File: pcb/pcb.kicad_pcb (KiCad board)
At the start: 2 copper layers, 190.5 x 85.7 mm, 55 parts, among them J1 OLED, SW1 Rotary_Encoder_Switch, U1 Elite-C

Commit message: Added initial modified files.
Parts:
- removed D1, D10, D11, D12, D13, D14, D15, D16, D2, D3, D4, D5, D6, D7, D8, D9: BAV70, Keebio-Parts:SOT-23_Handsoldering
- removed MX00, MX01, MX03, MX10, MX11, MX12, MX20, MX21, MX22, MX30, MX31, MX32, MX40, MX41, MX42, MX43, MX50, MX51, MX53, MX60, MX62, MX63, MX71, MX72: MX-NoLED, MX_Only:MXOnly-1U-Hotswap
- removed MX02, MX61: MX-NoLED, MX_Only:MXOnly-1.5U-Hotswap
- removed MX13, MX33: MX-NoLED, MX_Only:MXOnly-1.25U-Hotswap
- removed MX23: MX-NoLED, MX_Only:MXOnly-3U-Hotswap
- removed MX52: MX-NoLED, MX_Only:MXOnly-2U-Hotswap
- U1: footprint Keebio-Parts:Elite-C-castellated-29pin-holes -> Keebio-Parts:Elite-C
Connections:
- SW1 pad S1: Col7 -> unconnected-(SW1-PadS1)
- SW1 pad S2: Net-(D13-Pad2) -> unconnected-(SW1-PadS2)
- U1 pad 1: Col0 -> unconnected-(U1-Pad1)
- U1 pad 10: Col7 -> unconnected-(U1-Pad10)
- U1 pad 11: Row2 -> unconnected-(U1-Pad11)
- U1 pad 12: Row1 -> unconnected-(U1-Pad12)
- U1 pad 13: Row3 -> unconnected-(U1-Pad13)
- U1 pad 16: Col6 -> unconnected-(U1-Pad16)
- U1 pad 17: Col5 -> unconnected-(U1-Pad17)
- U1 pad 18: Col4 -> unconnected-(U1-Pad18)
- U1 pad 19: Col3 -> unconnected-(U1-Pad19)
- U1 pad 2: Col1 -> unconnected-(U1-Pad2)
- U1 pad 20: Col2 -> unconnected-(U1-Pad20)
- U1 pad 5: SDA -> unconnected-(U1-Pad5)
- U1 pad 6: SCL -> unconnected-(U1-Pad6)
- U1 pad 7: Row0 -> unconnected-(U1-Pad7)
- U1 pad 8: ENA -> unconnected-(U1-Pad8)
- U1 pad 9: ENB -> unconnected-(U1-Pad9)
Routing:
- net Row3: track 246.5 -> 0.00 mm, vias 1 -> 0
- net Col0: track 231.1 -> 0.00 mm, vias 4 -> 0
- net Col1: track 214.0 -> 0.00 mm, vias 4 -> 0
- net Col2: track 200.3 -> 0.00 mm, vias 4 -> 0
- net Col3: track 196.6 -> 0.00 mm, vias 4 -> 0
- net Col4: track 184.3 -> 0.00 mm, vias 4 -> 0
- net Row2: track 183.1 -> 0.00 mm, vias 1 -> 0
- net Row1: track 172.6 -> 0.00 mm, vias 1 -> 0
- net Row0: track 166.0 -> 0.00 mm, vias 2 -> 0
- net Col5: track 157.2 -> 0.00 mm, vias 4 -> 0
- net Col6: track 123.5 -> 0.00 mm, vias 4 -> 0
- net Col7: track 52.5 -> 0.00 mm, vias 2 -> 0
- net Net-(D14-Pad1): track 44.7 -> 0.00 mm
- net Net-(D13-Pad1): track 44.1 -> 0.00 mm, vias 2 -> 0
- net SDA: track 32.8 -> 0.00 mm, vias 1 -> 0
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
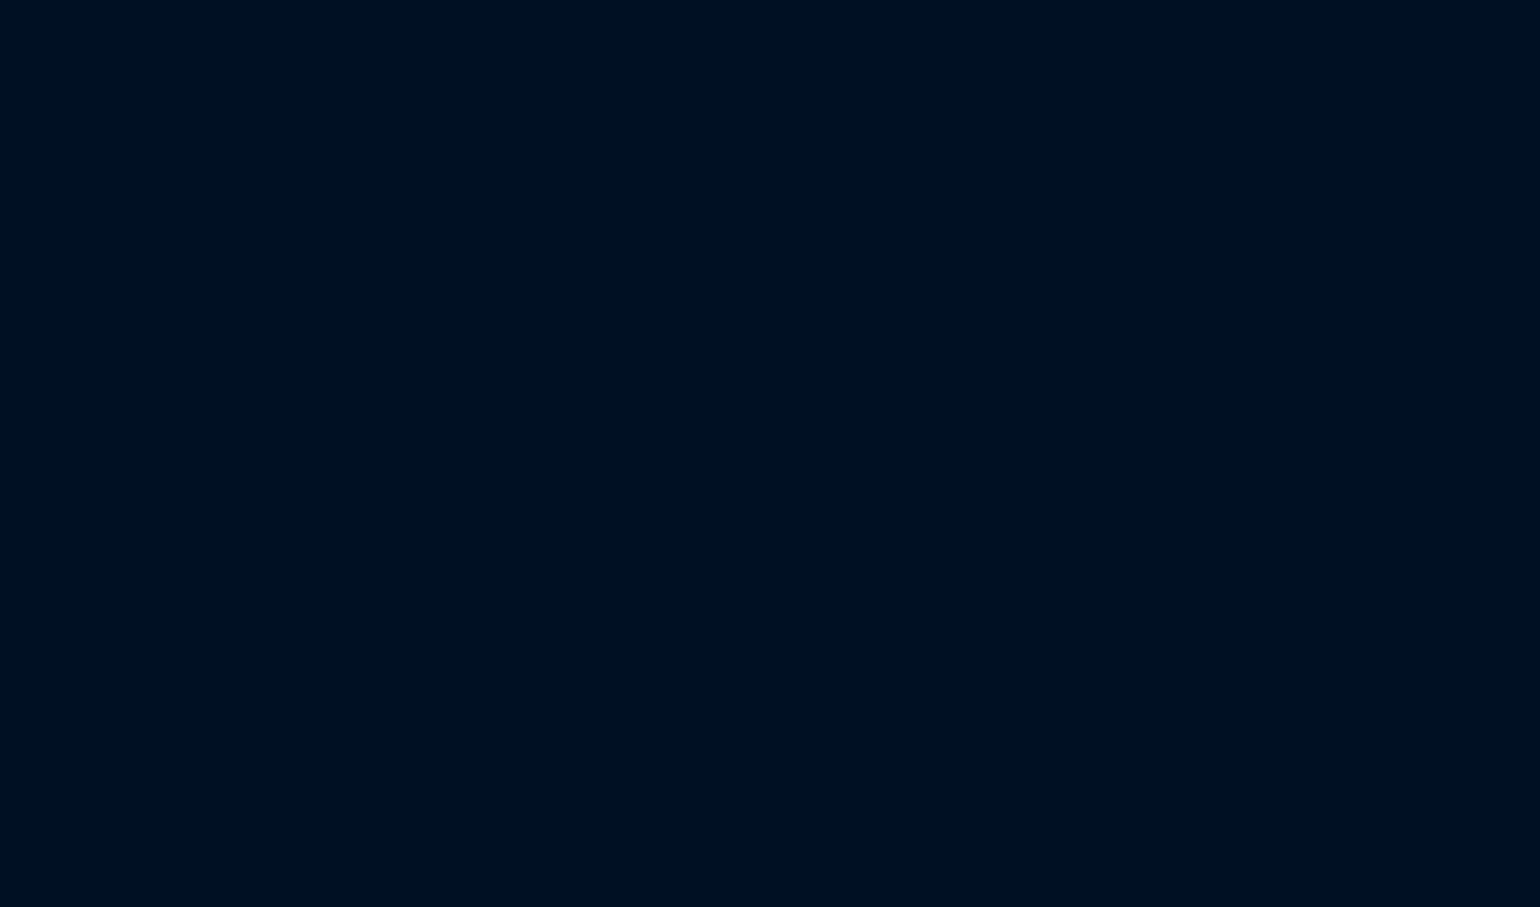
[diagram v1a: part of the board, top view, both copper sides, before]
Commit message: Finished tentative schematic and imported footprints into the PCB file.
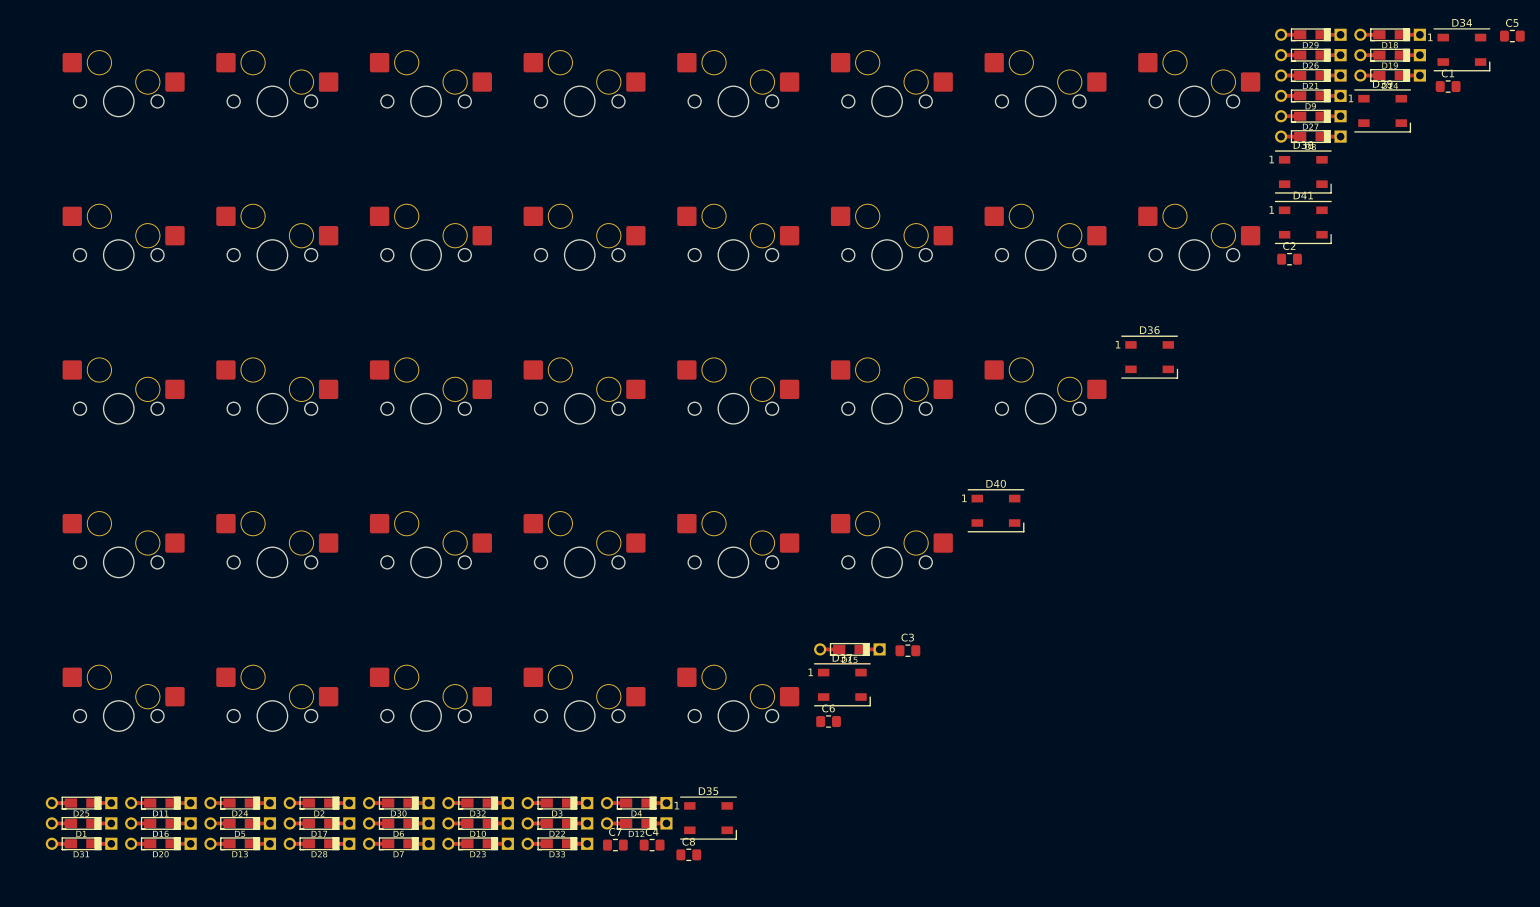
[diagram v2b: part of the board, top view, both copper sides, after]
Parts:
- added C1: 100n, Capacitor_SMD:C_0805_2012Metric_Pad1.18x1.45mm_HandSolder, F.Cu at (525.5, -42.9)
- added C2: 100n, Capacitor_SMD:C_0805_2012Metric_Pad1.18x1.45mm_HandSolder, F.Cu at (504.7, -20.2)
- added C3: 100n, Capacitor_SMD:C_0805_2012Metric_Pad1.18x1.45mm_HandSolder, F.Cu at (454.6, 31.1)
- added C4: 100n, Capacitor_SMD:C_0805_2012Metric_Pad1.18x1.45mm_HandSolder, F.Cu at (421.1, 56.6)
- added C5: 100n, Capacitor_SMD:C_0805_2012Metric_Pad1.18x1.45mm_HandSolder, F.Cu at (533.9, -49.5)
- added C6: 100n, Capacitor_SMD:C_0805_2012Metric_Pad1.18x1.45mm_HandSolder, F.Cu at (444.2, 40.4)
- added C7: 100n, Capacitor_SMD:C_0805_2012Metric_Pad1.18x1.45mm_HandSolder, F.Cu at (416.3, 56.6)
- added C8: 100n, Capacitor_SMD:C_0805_2012Metric_Pad1.18x1.45mm_HandSolder, F.Cu at (425.9, 57.9)
- added D1: D_Small, custom_parts:Diode-dual-onesided, F.Cu at (346.3, 53.8)
- added D10: D_Small, custom_parts:Diode-dual-onesided, F.Cu at (398.3, 53.8)
- added D11: D_Small, custom_parts:Diode-dual-onesided, F.Cu at (356.7, 51.1)
- added D12: D_Small, custom_parts:Diode-dual-onesided, F.Cu at (419.1, 53.8)
- added D13: D_Small, custom_parts:Diode-dual-onesided, F.Cu at (367.1, 56.4)
- added D14: D_Small, custom_parts:Diode-dual-onesided, F.Cu at (517.9, -44.3)
- added D15: D_Small, custom_parts:Diode-dual-onesided, F.Cu at (447.0, 30.9)
- added D16: D_Small, custom_parts:Diode-dual-onesided, F.Cu at (356.7, 53.8)
- added D17: D_Small, custom_parts:Diode-dual-onesided, F.Cu at (377.5, 53.8)
- added D18: D_Small, custom_parts:Diode-dual-onesided, F.Cu at (517.9, -49.7)
- added D19: D_Small, custom_parts:Diode-dual-onesided, F.Cu at (517.9, -47.0)
- added D2: D_Small, custom_parts:Diode-dual-onesided, F.Cu at (377.5, 51.1)
- added D20: D_Small, custom_parts:Diode-dual-onesided, F.Cu at (356.7, 56.4)
- added D21: D_Small, custom_parts:Diode-dual-onesided, F.Cu at (507.5, -44.3)
- added D22: D_Small, custom_parts:Diode-dual-onesided, F.Cu at (408.7, 53.8)
- added D23: D_Small, custom_parts:Diode-dual-onesided, F.Cu at (398.3, 56.4)
- added D24: D_Small, custom_parts:Diode-dual-onesided, F.Cu at (367.1, 51.1)
- added D25: D_Small, custom_parts:Diode-dual-onesided, F.Cu at (346.3, 51.1)
- added D26: D_Small, custom_parts:Diode-dual-onesided, F.Cu at (507.5, -47.0)
- added D27: D_Small, custom_parts:Diode-dual-onesided, F.Cu at (507.5, -39.0)
- added D28: D_Small, custom_parts:Diode-dual-onesided, F.Cu at (377.5, 56.4)
- added D29: D_Small, custom_parts:Diode-dual-onesided, F.Cu at (507.5, -49.7)
- added D3: D_Small, custom_parts:Diode-dual-onesided, F.Cu at (408.7, 51.1)
- added D30: D_Small, custom_parts:Diode-dual-onesided, F.Cu at (387.9, 51.1)
- added D31: D_Small, custom_parts:Diode-dual-onesided, F.Cu at (346.3, 56.4)
- added D32: D_Small, custom_parts:Diode-dual-onesided, F.Cu at (398.3, 51.1)
- added D33: D_Small, custom_parts:Diode-dual-onesided, F.Cu at (408.7, 56.4)
- added D34: WS2812B, LED_SMD:LED_WS2812B_PLCC4_5.0x5.0mm_P3.2mm, F.Cu at (527.3, -47.7)
- added D35: WS2812B, LED_SMD:LED_WS2812B_PLCC4_5.0x5.0mm_P3.2mm, F.Cu at (428.5, 53.1)
- added D36: WS2812B, LED_SMD:LED_WS2812B_PLCC4_5.0x5.0mm_P3.2mm, F.Cu at (486.3, -7.38)
- added D37: WS2812B, LED_SMD:LED_WS2812B_PLCC4_5.0x5.0mm_P3.2mm, F.Cu at (446.0, 35.6)
- added D38: WS2812B, LED_SMD:LED_WS2812B_PLCC4_5.0x5.0mm_P3.2mm, F.Cu at (506.5, -31.7)
- added D39: WS2812B, LED_SMD:LED_WS2812B_PLCC4_5.0x5.0mm_P3.2mm, F.Cu at (516.9, -39.7)
- added D4: D_Small, custom_parts:Diode-dual-onesided, F.Cu at (419.1, 51.1)
- added D40: WS2812B, LED_SMD:LED_WS2812B_PLCC4_5.0x5.0mm_P3.2mm, F.Cu at (466.2, 12.8)
- added D41: WS2812B, LED_SMD:LED_WS2812B_PLCC4_5.0x5.0mm_P3.2mm, F.Cu at (506.5, -25.0)
- added D5: D_Small, custom_parts:Diode-dual-onesided, F.Cu at (367.1, 53.8)
- added D6: D_Small, custom_parts:Diode-dual-onesided, F.Cu at (387.9, 53.8)
- added D7: D_Small, custom_parts:Diode-dual-onesided, F.Cu at (387.9, 56.4)
- added D8: D_Small, custom_parts:Diode-dual-onesided, F.Cu at (507.5, -36.3)
- added D9: D_Small, custom_parts:Diode-dual-onesided, F.Cu at (507.5, -41.6)
- added MX1: Esc/e0, acheron_MXH_metalrings:MX100H, F.Cu at (371.3, -20.8)
- added MX10: R, acheron_MXH_metalrings:MX100H, F.Cu at (351.1, -20.8)
- added MX11: F5, acheron_MXH_metalrings:MX100H, F.Cu at (431.7, -40.9)
- added MX12: Insert, acheron_MXH_metalrings:MX100H, F.Cu at (492.2, -20.8)
- added MX13: Shift, acheron_MXH_metalrings:MX100H, F.Cu at (371.3, 39.7)
- added MX14: W, acheron_MXH_metalrings:MX100H, F.Cu at (451.9, -40.9)
- added MX15: D, acheron_MXH_metalrings:MX100H, F.Cu at (431.7, -20.8)
- added MX16: T, acheron_MXH_metalrings:MX100H, F.Cu at (431.7, 19.5)
- added MX17: F6, acheron_MXH_metalrings:MX100H, F.Cu at (351.1, -0.61)
- added MX18: Delete, acheron_MXH_metalrings:MX100H, F.Cu at (431.7, -0.61)
- added MX19: Ctrl, acheron_MXH_metalrings:MX100H, F.Cu at (411.6, -0.61)
- added MX2: F1, acheron_MXH_metalrings:MX100H, F.Cu at (391.4, -20.8)
- added MX20: S, acheron_MXH_metalrings:MX100H, F.Cu at (472.0, -0.61)
- added MX21: F, acheron_MXH_metalrings:MX100H, F.Cu at (391.4, 19.5)
- added MX22: G, acheron_MXH_metalrings:MX100H, F.Cu at (351.1, 39.7)
- added MX23: Bspc, acheron_MXH_metalrings:MX100H, F.Cu at (411.6, 39.7)
- added MX24: Left, acheron_MXH_metalrings:MX100H, F.Cu at (391.4, -0.61)
- added MX25: Alt, acheron_MXH_metalrings:MX100H, F.Cu at (391.4, -40.9)
- added MX26: Space, acheron_MXH_metalrings:MX100H, F.Cu at (371.3, -0.61)
- added MX27: Ctrl, acheron_MXH_metalrings:MX100H, F.Cu at (472.0, -20.8)
- added MX28: Right, acheron_MXH_metalrings:MX100H, F.Cu at (472.0, -40.9)
- added MX29: Enter ISO, acheron_MXH_metalrings:MX100H, F.Cu at (451.9, 19.5)
- added MX3: F2, acheron_MXH_metalrings:MX100H, F.Cu at (431.7, 39.7)
- added MX30: Enter ANSI, acheron_MXH_metalrings:MX100H, F.Cu at (371.3, -40.9)
- added MX31: A, acheron_MXH_metalrings:MX100H, F.Cu at (351.1, -40.9)
- added MX32: Alt, acheron_MXH_metalrings:MX100H, F.Cu at (492.2, -40.9)
- added MX33: Down, acheron_MXH_metalrings:MX100H, F.Cu at (371.3, 19.5)
- added MX34: Up, acheron_MXH_metalrings:MX100H, F.Cu at (351.1, 19.5)
- added MX4: F3, acheron_MXH_metalrings:MX100H, F.Cu at (411.6, 19.5)
- added MX5: F4, acheron_MXH_metalrings:MX100H, F.Cu at (391.4, 39.7)
- added MX6: Mute/e1, acheron_MXH_metalrings:MX100H, F.Cu at (411.6, -40.9)
- added MX7: Tab, acheron_MXH_metalrings:MX100H, F.Cu at (451.9, -20.8)
- added MX8: Q, acheron_MXH_metalrings:MX100H, F.Cu at (451.9, -0.61)
- added MX9: E, acheron_MXH_metalrings:MX100H, F.Cu at (411.6, -20.8)
- SW1: value Rotary_Encoder_Switch -> RotaryEncoder_Switch
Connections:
- SW1 pad A: ENB -> ENA
- SW1 pad B: ENA -> ENB
- SW1 pad S1: unconnected-(SW1-PadS1) -> COL0
- SW1 pad S2: unconnected-(SW1-PadS2) -> ROW0
- U1 pad 1: unconnected-(U1-Pad1) -> ROW0
- U1 pad 10: unconnected-(U1-Pad10) -> ROW5
- U1 pad 11: unconnected-(U1-Pad11) -> COL0
- U1 pad 12: unconnected-(U1-Pad12) -> COL1
- U1 pad 14: unconnected-(U1-Pad14) -> UGLOW
- U1 pad 15: unconnected-(U1-Pad15) -> ENB
- U1 pad 16: unconnected-(U1-Pad16) -> ENA
- U1 pad 17: unconnected-(U1-Pad17) -> COL5
- U1 pad 18: unconnected-(U1-Pad18) -> COL4
- U1 pad 19: unconnected-(U1-Pad19) -> COL3
- U1 pad 2: unconnected-(U1-Pad2) -> ROW1
- U1 pad 20: unconnected-(U1-Pad20) -> COL2
- U1 pad 5: unconnected-(U1-Pad5) -> SDA
- U1 pad 6: unconnected-(U1-Pad6) -> SCL
- U1 pad 7: unconnected-(U1-Pad7) -> ROW2
- U1 pad 8: unconnected-(U1-Pad8) -> ROW3
- U1 pad 9: unconnected-(U1-Pad9) -> ROW4

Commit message: Modified Elite-C footprint.
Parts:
- C1, C2, C3, C4, C5, C6, C7, C8, D1, D10, D11, D12, D13, D14, D15, D16, D17, D18, D19, D2, D20, D21, D22, D23, D24, D25, D26, D27, D28, D29, D3, D30, D31, D32, D33, D34, D35, D36, D37, D38, D39, D4, D40, D41, D5, D6, D7, D8, D9, MX1, MX10, MX11, MX12, MX13, MX14, MX15, MX16, MX17, MX18, MX19, MX2, MX20, MX21, MX22, MX23, MX24, MX25, MX26, MX27, MX28, MX29, MX3, MX30, MX31, MX32, MX33, MX34, MX4, MX5, MX6, MX7, MX8, MX9: moved to B.Cu
- U1: footprint Keebio-Parts:Elite-C -> Keebio-Parts:Elite-C-castellated-29pin-holes
- moved MX3 365.4 mm to (66.7, 23.8), turned to 180 degrees
- moved MX1 350.3 mm to (23.8, 23.8), turned to 180 degrees
- moved MX2 346.7 mm to (47.6, 23.8), turned to 180 degrees
- moved MX4 325.9 mm to (85.7, 23.8), turned to 180 degrees
- moved MX11 310.0 mm to (128.6, 23.8), turned to 180 degrees
- moved MX5 282.3 mm to (109.5, 23.8), turned to 180 degrees
- moved MX6 225.8 mm to (195.3, 23.8), turned to 180 degrees
- moved MX17 205.0 mm to (147.6, 23.8), turned to 180 degrees
- moved C5 190.4 mm to (343.5, -49.5), turned to 180 degrees
- moved D1 184.9 mm to (531.1, 53.8), turned to 180 degrees
- moved D25 184.9 mm to (531.1, 51.1), turned to 180 degrees
- moved D31 184.9 mm to (531.1, 56.4), turned to 180 degrees
- moved D34 177.1 mm to (350.1, -47.7), turned to 180 degrees
- moved MX10 175.1 mm to (526.3, -20.8), turned to 180 degrees
- moved MX22 175.1 mm to (526.3, 39.7), turned to 180 degrees
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
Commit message: Added footprints for most of the parts to the PCB file.
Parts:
- added S1: MX_stab, marbastlib-mx:STAB_MX_2.25u, F.Cu at (135.7, 66.7)
- added S2: MX_stab, marbastlib-mx:STAB_MX_ISO_FLIPPED, F.Cu at (145.3, 57.1)
- MX13, MX25, MX32: footprint acheron_MXH_metalrings:MX100H -> acheron_MXH_metalrings:MX125H
- MX26: footprint acheron_MXH_metalrings:MX100H -> acheron_MXH_metalrings:MX200H
- SW1: footprint Rotary_Encoder:RotaryEncoder_Alps_EC11E-Switch_Vertical_H20mm -> Keebio-Parts:RotaryEncoder_EC11-no-legs
- moved D1 497.9 mm to (34.1, 23.8), turned to -90 degrees
- moved D25 497.2 mm to (35.2, 85.7), turned to -90 degrees
- moved D13 494.4 mm to (16.0, 66.7), turned to -90 degrees
- moved MX31 490.6 mm to (47.6, 66.7)
- moved MX13 480.7 mm to (26.2, 66.7)
- moved D20 464.3 mm to (56.5, 66.7), turned to -90 degrees
- moved D2 463.4 mm to (37.3, 23.8), turned to -90 degrees
- moved MX25 458.6 mm to (45.2, 85.7)
- moved D7 456.9 mm to (32.8, 47.6), turned to -90 degrees
- moved D30 452.3 mm to (37.5, 66.7), turned to -90 degrees
- moved MX19 450.4 mm to (23.8, 85.7)
- moved MX26 438.5 mm to (76.2, 85.7)
- moved D31 436.0 mm to (96.1, 85.7), turned to -90 degrees
- moved MX10 431.7 mm to (100.0, 47.6)
- moved D5 413.9 mm to (97.5, 23.9), turned to -90 degrees
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
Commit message: Added missing LEDs and caps.
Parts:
- added C10: 100n, Capacitor_SMD:C_0805_2012Metric_Pad1.18x1.45mm_HandSolder, B.Cu at (37.0, 53.3)
- added C9: 100n, Capacitor_SMD:C_0805_2012Metric_Pad1.18x1.45mm_HandSolder, B.Cu at (32.6, 75.7)
- added D42: WS2812B, LED_SMD:LED_WS2812B_PLCC4_5.0x5.0mm_P3.2mm, B.Cu at (37.2, 75.7)
- added D43: WS2812B, LED_SMD:LED_WS2812B_PLCC4_5.0x5.0mm_P3.2mm, B.Cu at (37.0, 57.1)
- moved C8 322.2 mm to (81.2, 71.8)
- moved C1 317.8 mm to (35.4, 32.3)
- moved C7 274.5 mm to (138.7, 72.3)
- moved C2 244.4 mm to (86.0, 32.3)
- moved C3 236.2 mm to (138.0, 32.3)
- moved C4 222.0 mm to (186.9, 32.3)
- moved C6 203.9 mm to (184.1, 75.0)
- moved C5 182.6 mm to (185.5, 60.6)
- moved H4 16.8 mm to (198.9, 76.2)
- moved H2 10.1 mm to (23.2, 76.2)
- moved D39 5.26 mm to (184.1, 78.9)
- moved D38 3.72 mm to (185.7, 56.6)
- moved H1 3.51 mm to (23.2, 35.7)
- moved D37 2.41 mm to (186.9, 36.1)
- moved D41 1.55 mm to (81.2, 75.6)
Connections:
- D38 pad 2: unconnected-(D38-Pad2) -> Net-(D38-Pad2)
